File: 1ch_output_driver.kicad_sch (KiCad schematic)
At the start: 3 parts, among them U8 LTV-817S

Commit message: tidy of some sheets. Added 0-10V DAC, but untested - only some basic validation on simulator for now
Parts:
- U8: footprint Package_DIP:SMDIP-4_W9.53mm -> Package_SO:SOIC-16_3.9x9.9mm_P1.27mm
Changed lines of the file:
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@@
 			)
 		)
-		(property "Footprint" "Package_DIP:SMDIP-4_W9.53mm"
+		(property "Footprint" "Package_SO:SOIC-16_3.9x9.9mm_P1.27mm"
 			(at 140.97 102.87 0)
 			(effects

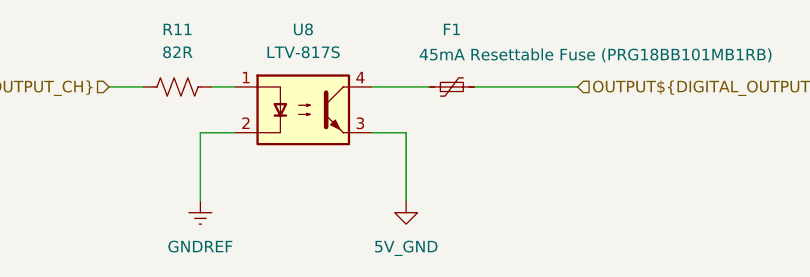
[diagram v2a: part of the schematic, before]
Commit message: restructured power supplies to enable Spindle DAC to be isolated. We now have the option of supplying two 24V inputs, one to power the nucleo and everything logic side and the other to power peripherals. Some testing will be required.
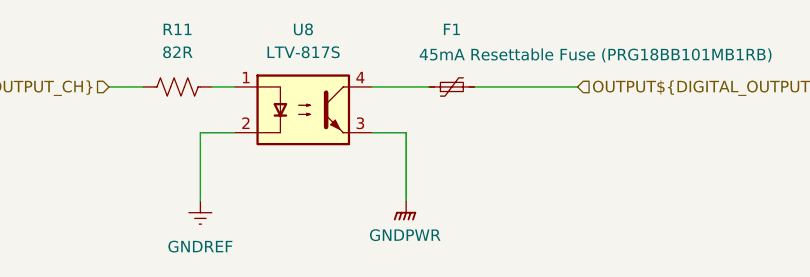
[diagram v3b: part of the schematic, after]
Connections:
- net 5V_GND renamed GNDPWR
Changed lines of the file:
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@@
-	)
-	(symbol
-		(lib_id "power:GND1")
-		(at 152.4 105.41 0)
-		(unit 1)
-		(exclude_from_sim no)
-		(in_bom yes)
-		(on_board yes)
-		(dnp no)
-		(fields_autoplaced yes)
-		(property "Reference" "#PWR071"
-			(at 152.4 111.76 0)
-			(effects
-				(font
-					(size 1.27 1.27)
-				)
-				(hide yes)
-			)
-		)
-		(property "Value" "5V_GND"
-			(at 152.4 110.49 0)
-			(effects
-				(font
-					(size 1.27 1.27)
-				)
-			)
-		)
-		(property "Footprint" ""
-			(at 152.4 105.41 0)
-			(effects
-				(font
-					(size 1.27 1.27)
-				)
-				(hide yes)
-			)
-		)
-		(property "Datasheet" ""
-			(at 152.4 105.41 0)
-			(effects
-				(font
-					(size 1.27 1.27)
-				)
-				(hide yes)
-			)
-		)
-		(property "Description" "Power symbol creates a global label with name \"GND1\" , ground"
-			(at 152.4 105.41 0)
-			(effects
-				(font
-					(size 1.27 1.27)
-				)
-				(hide yes)
-			)
-		)
-		(pin "1"
-		)
-		(instances
-			(project "Remora Nucleo F446ZE Hat"
-				(path "/5473abc6-7b93-43cc-a401-f691c4d7d7cf/a10f9653-3098-46b3-8571-958500eea49a/262aff85-41f1-4da9-8699-86dfa1e841b0"
-					(reference "#PWR0130")
-					(unit 1)
-				)
-				(path "/5473abc6-7b93-43cc-a401-f691c4d7d7cf/a10f9653-3098-46b3-8571-958500eea49a/455c10af-7b62-4794-9ad7-d5e1944edd00"
-					(reference "#PWR073")
-					(unit 1)
-				)
-				(path "/5473abc6-7b93-43cc-a401-f691c4d7d7cf/a10f9653-3098-46b3-8571-958500eea49a/49370d92-281f-43fd-85e2-bd3930420692"
-					(reference "#PWR0134")
-					(unit 1)
-				)
-				(path "/5473abc6-7b93-43cc-a401-f691c4d7d7cf/a10f9653-3098-46b3-8571-958500eea49a/511cd8b7-3e67-472f-9a06-23d9f7789ea5"
-					(reference "#PWR081")
-					(unit 1)
-				)
-				(path "/5473abc6-7b93-43cc-a401-f691c4d7d7cf/a10f9653-3098-46b3-8571-958500eea49a/75bfee9f-dba1-4332-b42b-f74c9030c21f"
-					(reference "#PWR071")
-					(unit 1)
-				)
-				(path "/5473abc6-7b93-43cc-a401-f691c4d7d7cf/a10f9653-3098-46b3-8571-958500eea49a/7e7c735f-9b06-4a77-82b5-cd52d4798a5a"
-					(reference "#PWR075")
-					(unit 1)
-				)
-				(path "/5473abc6-7b93-43cc-a401-f691c4d7d7cf/a10f9653-3098-46b3-8571-958500eea49a/be37db14-01b9-4658-a2ab-e736ce09f7af"
-					(reference "#PWR0128")
-					(unit 1)
-				)
-				(path "/5473abc6-7b93-43cc-a401-f691c4d7d7cf/a10f9653-3098-46b3-8571-958500eea49a/c9335f60-c03a-4512-bd65-d0261a984930"
-					(reference "#PWR077")
-					(unit 1)
-				)
-				(path "/5473abc6-7b93-43cc-a401-f691c4d7d7cf/a10f9653-3098-46b3-8571-958500eea49a/dcb3f0e6-0f43-4944-b372-1b15f6985d9f"
-					(reference "#PWR0132")
-					(unit 1)
-				)
-				(path "/5473abc6-7b93-43cc-a401-f691c4d7d7cf/a10f9653-3098-46b3-8571-958500eea49a/fe21da7f-7aa5-41b9-995f-11902d4a289b"
-					(reference "#PWR079")
-					(unit 1)
-				)
-			)
-		)
 	)
 	(symbol
@@
 					(unit 1)
 				)
+			)
+		)
+	)
+	(symbol
+		(lib_id "power:GNDPWR")
+		(at 152.4 105.41 0)
+		(unit 1)
+		(exclude_from_sim no)
+		(in_bom yes)
+		(on_board yes)
+		(dnp no)
+		(fields_autoplaced yes)
+		(property "Reference" "#PWR0121"
+			(at 152.4 110.49 0)
+			(effects
+				(font
+					(size 1.27 1.27)
+				)
+				(hide yes)
+			)
+		)
+		(property "Value" "GNDPWR"
+			(at 152.273 109.22 0)
+			(effects
+				(font
+					(size 1.27 1.27)
+				)
+			)
+		)
+		(property "Footprint" ""
+			(at 152.4 106.68 0)
+			(effects
+				(font
+					(size 1.27 1.27)
+				)
+				(hide yes)
+			)
+		)
+		(property "Datasheet" ""
+			(at 152.4 106.68 0)
+			(effects
+				(font
+					(size 1.27 1.27)
+				)
+				(hide yes)
+			)
+		)
+		(property "Description" "Power symbol creates a global label with name \"GNDPWR\" , global ground"
+			(at 152.4 105.41 0)
+			(effects
+				(font
+					(size 1.27 1.27)
+				)
+				(hide yes)
+			)
+		)
+		(pin "1"
+		)
+		(instances
+			(project "Remora Nucleo F446ZE Hat"
+				(path "/5473abc6-7b93-43cc-a401-f691c4d7d7cf/a10f9653-3098-46b3-8571-958500eea49a/262aff85-41f1-4da9-8699-86dfa1e841b0"
+					(reference "#PWR0236")
+					(unit 1)
+				)
+				(path "/5473abc6-7b93-43cc-a401-f691c4d7d7cf/a10f9653-3098-46b3-8571-958500eea49a/455c10af-7b62-4794-9ad7-d5e1944edd00"
+					(reference "#PWR0135")
+					(unit 1)
+				)
+				(path "/5473abc6-7b93-43cc-a401-f691c4d7d7cf/a10f9653-3098-46b3-8571-958500eea49a/49370d92-281f-43fd-85e2-bd3930420692"
+					(reference "#PWR0238")
+					(unit 1)
+				)
+				(path "/5473abc6-7b93-43cc-a401-f691c4d7d7cf/a10f9653-3098-46b3-8571-958500eea49a/511cd8b7-3e67-472f-9a06-23d9f7789ea5"
+					(reference "#PWR0234")
+					(unit 1)
+				)
+				(path "/5473abc6-7b93-43cc-a401-f691c4d7d7cf/a10f9653-3098-46b3-8571-958500eea49a/75bfee9f-dba1-4332-b42b-f74c9030c21f"
+					(reference "#PWR0121")
+					(unit 1)
+				)
+				(path "/5473abc6-7b93-43cc-a401-f691c4d7d7cf/a10f9653-3098-46b3-8571-958500eea49a/7e7c735f-9b06-4a77-82b5-cd52d4798a5a"
+					(reference "#PWR0137")
+					(unit 1)
+				)
+				(path "/5473abc6-7b93-43cc-a401-f691c4d7d7cf/a10f9653-3098-46b3-8571-958500eea49a/be37db14-01b9-4658-a2ab-e736ce09f7af"
+					(reference "#PWR0235")
+					(unit 1)
+				)
+				(path "/5473abc6-7b93-43cc-a401-f691c4d7d7cf/a10f9653-3098-46b3-8571-958500eea49a/c9335f60-c03a-4512-bd65-d0261a984930"
+					(reference "#PWR0141")
+					(unit 1)
+				)
+				(path "/5473abc6-7b93-43cc-a401-f691c4d7d7cf/a10f9653-3098-46b3-8571-958500eea49a/dcb3f0e6-0f43-4944-b372-1b15f6985d9f"
+					(reference "#PWR0237")
+					(unit 1)
+				)
+				(path "/5473abc6-7b93-43cc-a401-f691c4d7d7cf/a10f9653-3098-46b3-8571-958500eea49a/fe21da7f-7aa5-41b9-995f-11902d4a289b"
+					(reference "#PWR0232")
+					(unit 1)
+				)

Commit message: Fixed bug with lack of pin header for CN11 and CN12. Addeded RPI header and aligned it, assigned some safe footprints
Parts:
- R11: footprint (none) -> Resistor_SMD:R_1206_3216Metric_Pad1.30x1.75mm_HandSolder
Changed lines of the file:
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@@
 			)
 		)
-		(property "Footprint" ""
+		(property "Footprint" "Resistor_SMD:R_1206_3216Metric_Pad1.30x1.75mm_HandSolder"
 			(at 127.254 91.694 90)
 			(effects

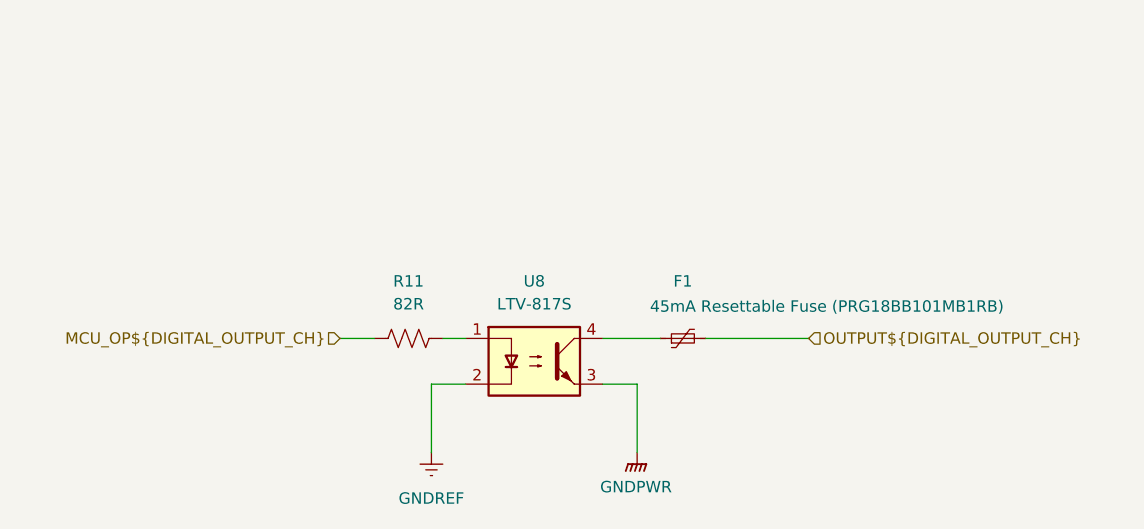
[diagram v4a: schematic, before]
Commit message: updates to read me, marked V1 parts inactive and made start on board layout for initial test board. fixes to BOM to suit
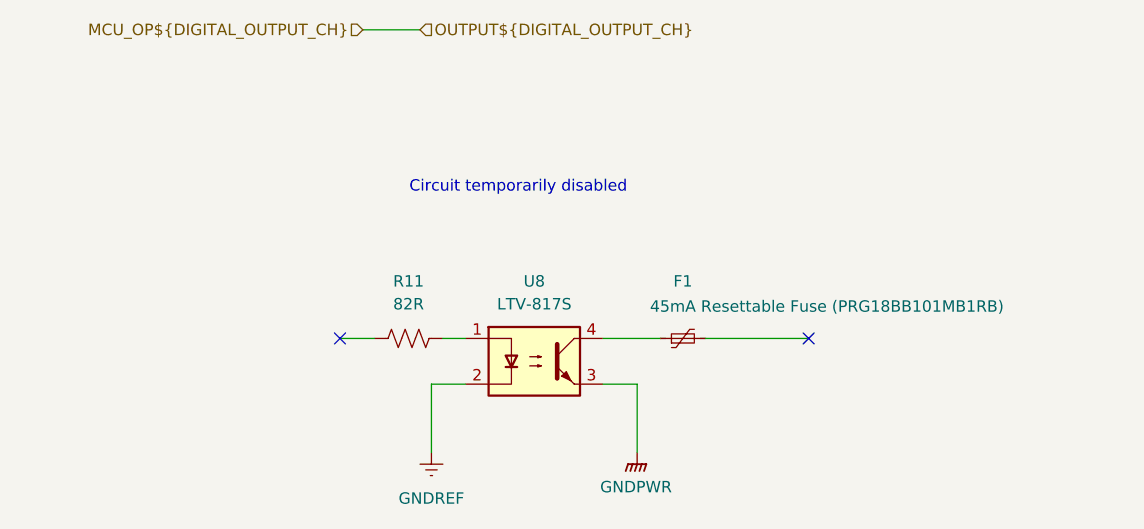
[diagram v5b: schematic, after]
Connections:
- net MCU_OP${DIGITAL_OUTPUT_CH}: no longer R11.1
- net OUTPUT${DIGITAL_OUTPUT_CH}: no longer names the net of F1.2
- no-connect marks 0 -> 2
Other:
- note added: "Circuit temporarily disabled"
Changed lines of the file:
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@@
 	(generator_version "9.0")
 	(paper "A4")
-	(wire
-		(pts
-			(xy 152.4 97.79) (xy 152.4 105.41)
-		)
-		(stroke
-			(width 0)
-			(type default)
-		)
-	)
-	(wire
-		(pts
-			(xy 148.59 92.71) (xy 154.94 92.71)
-		)
-		(stroke
-			(width 0)
-			(type default)
-		)
-	)
-	(wire
-		(pts
-			(xy 123.19 92.71) (xy 119.38 92.71)
-		)
-		(stroke
-			(width 0)
-			(type default)
-		)
-	)
-	(wire
-		(pts
-			(xy 130.81 92.71) (xy 133.35 92.71)
-		)
-		(stroke
-			(width 0)
-			(type default)
-		)
-	)
-	(wire
-		(pts
-			(xy 148.59 97.79) (xy 152.4 97.79)
-		)
-		(stroke
-			(width 0)
-			(type default)
-		)
-	)
-	(wire
-		(pts
-			(xy 160.02 92.71) (xy 171.45 92.71)
-		)
-		(stroke
-			(width 0)
-			(type default)
-		)
-	)
-	(wire
-		(pts
-			(xy 129.54 97.79) (xy 129.54 105.41)
-		)
-		(stroke
-			(width 0)
-			(type default)
-		)
-	)
-	(wire
-		(pts
-			(xy 129.54 97.79) (xy 133.35 97.79)
-		)
-		(stroke
-			(width 0)
-			(type default)
-		)
-	)
-	(hierarchical_label "MCU_OP${DIGITAL_OUTPUT_CH}"
-		(shape input)
-		(at 119.38 92.71 180)
+	(text "Circuit temporarily disabled\n"
+		(exclude_from_sim no)
+		(at 139.192 75.946 0)
 		(effects
 			(font
 				(size 1.27 1.27)
 			)
+		)
+	)
+	(no_connect
+		(at 171.45 92.71)
+	)
+	(no_connect
+		(at 119.38 92.71)
+	)
+	(wire
+		(pts
+			(xy 121.92 58.42) (xy 128.27 58.42)
+		)
+		(stroke
+			(width 0)
+			(type default)
+		)
+	)
+	(wire
+		(pts
+			(xy 152.4 97.79) (xy 152.4 105.41)
+		)
+		(stroke
+			(width 0)
+			(type default)
+		)
+	)
+	(wire
+		(pts
+			(xy 148.59 92.71) (xy 154.94 92.71)
+		)
+		(stroke
+			(width 0)
+			(type default)
+		)
+	)
+	(wire
+		(pts
+			(xy 123.19 92.71) (xy 119.38 92.71)
+		)
+		(stroke
+			(width 0)
+			(type default)
+		)
+	)
+	(wire
+		(pts
+			(xy 130.81 92.71) (xy 133.35 92.71)
+		)
+		(stroke
+			(width 0)
+			(type default)
+		)
+	)
+	(wire
+		(pts
+			(xy 148.59 97.79) (xy 152.4 97.79)
+		)
+		(stroke
+			(width 0)
+			(type default)
+		)
+	)
+	(wire
+		(pts
+			(xy 160.02 92.71) (xy 171.45 92.71)
+		)
+		(stroke
+			(width 0)
+			(type default)
+		)
+	)
+	(wire
+		(pts
+			(xy 129.54 97.79) (xy 129.54 105.41)
+		)
+		(stroke
+			(width 0)
+			(type default)
+		)
+	)
+	(wire
+		(pts
+			(xy 129.54 97.79) (xy 133.35 97.79)
+		)
+		(stroke
+			(width 0)
+			(type default)
+		)
+	)
+	(hierarchical_label "MCU_OP${DIGITAL_OUTPUT_CH}"
+		(shape input)
+		(at 121.92 58.42 180)
+		(effects
+			(font
+				(size 1.27 1.27)
+			)
 			(justify right)
 		)
@@
 	(hierarchical_label "OUTPUT${DIGITAL_OUTPUT_CH}"
 		(shape input)
-		(at 171.45 92.71 0)
+		(at 128.27 58.42 0)
 		(effects
 			(font
@@
 		(exclude_from_sim no)
 		(in_bom yes)
-		(on_board yes)
+		(on_board no)
 		(dnp no)
 		(property "Reference" "F1"
@@
 		(exclude_from_sim no)
 		(in_bom yes)
-		(on_board yes)
+		(on_board no)
 		(dnp no)
 		(fields_autoplaced yes)
@@
 		(exclude_from_sim no)
 		(in_bom yes)
-		(on_board yes)
+		(on_board no)
 		(dnp no)
 		(fields_autoplaced yes)
